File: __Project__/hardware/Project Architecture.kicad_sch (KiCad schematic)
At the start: 0 parts

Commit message: Different fixes and new footprints
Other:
- note added: "Page 7"
- note added: "Page 8"
- note removed: "Page 4"
- note removed: "Page 5"
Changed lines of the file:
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@@
 		)
 	)
-	(text "Page 5"
+	(text "Page 8"
 		(exclude_from_sim no)
 		(at 226.06 133.35 0)
@@
 			)
 			(justify right bottom)
-			(href "#5")
+			(href "#8")
 		)
 	)
-	(text "Page 4"
+	(text "Page 7"
 		(exclude_from_sim no)
 		(at 226.06 95.25 0)
@@
 			)
 			(justify right bottom)
-			(href "#4")
+			(href "#7")
 		)
 	)

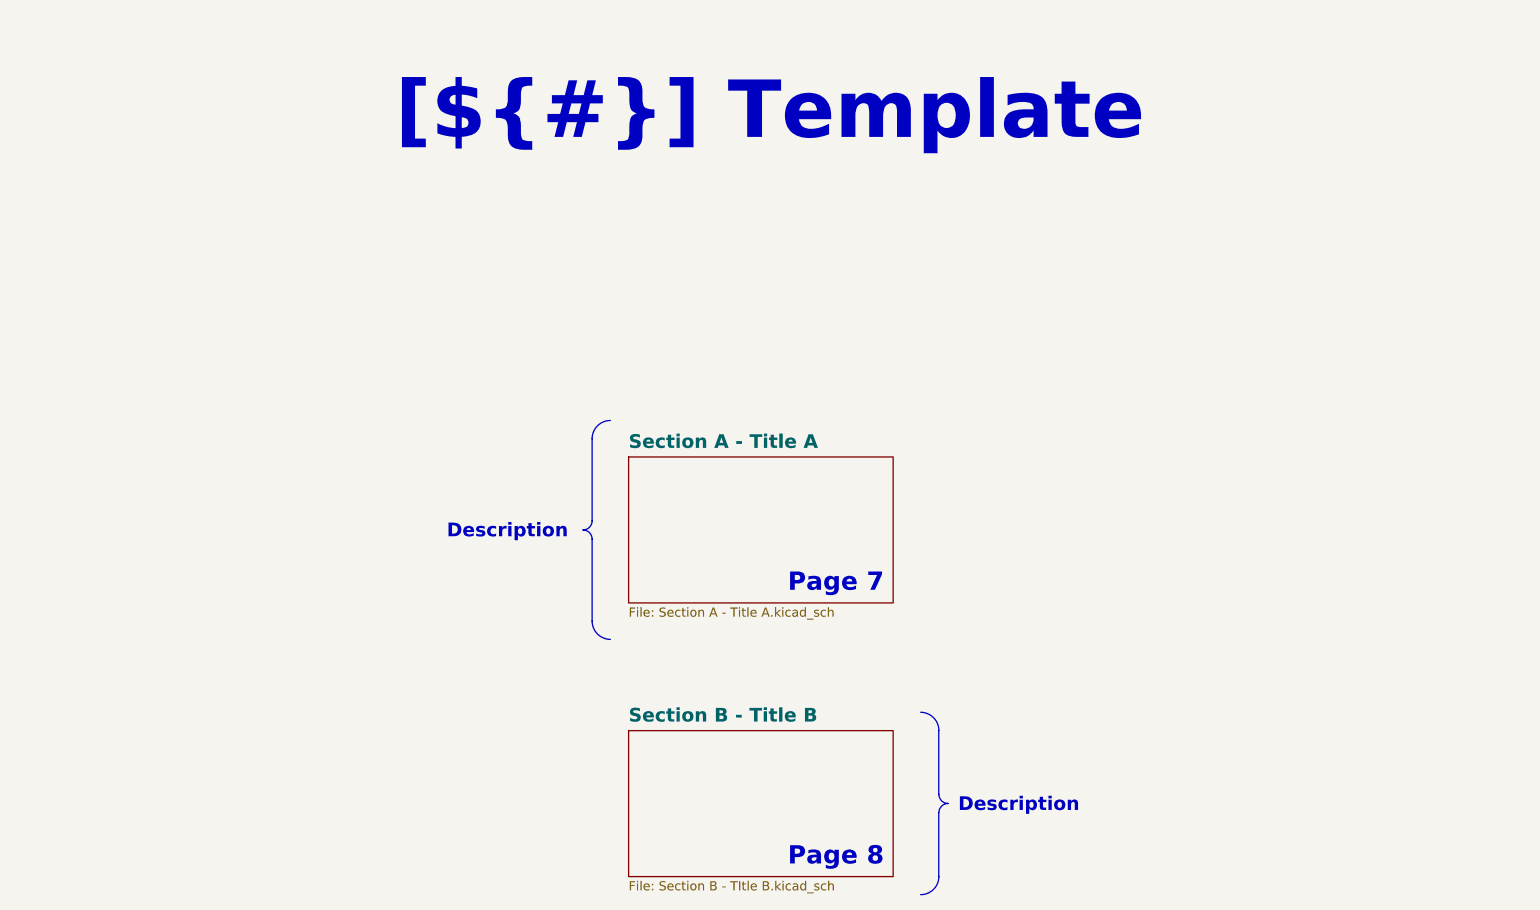
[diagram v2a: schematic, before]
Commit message: Fix JST footprints
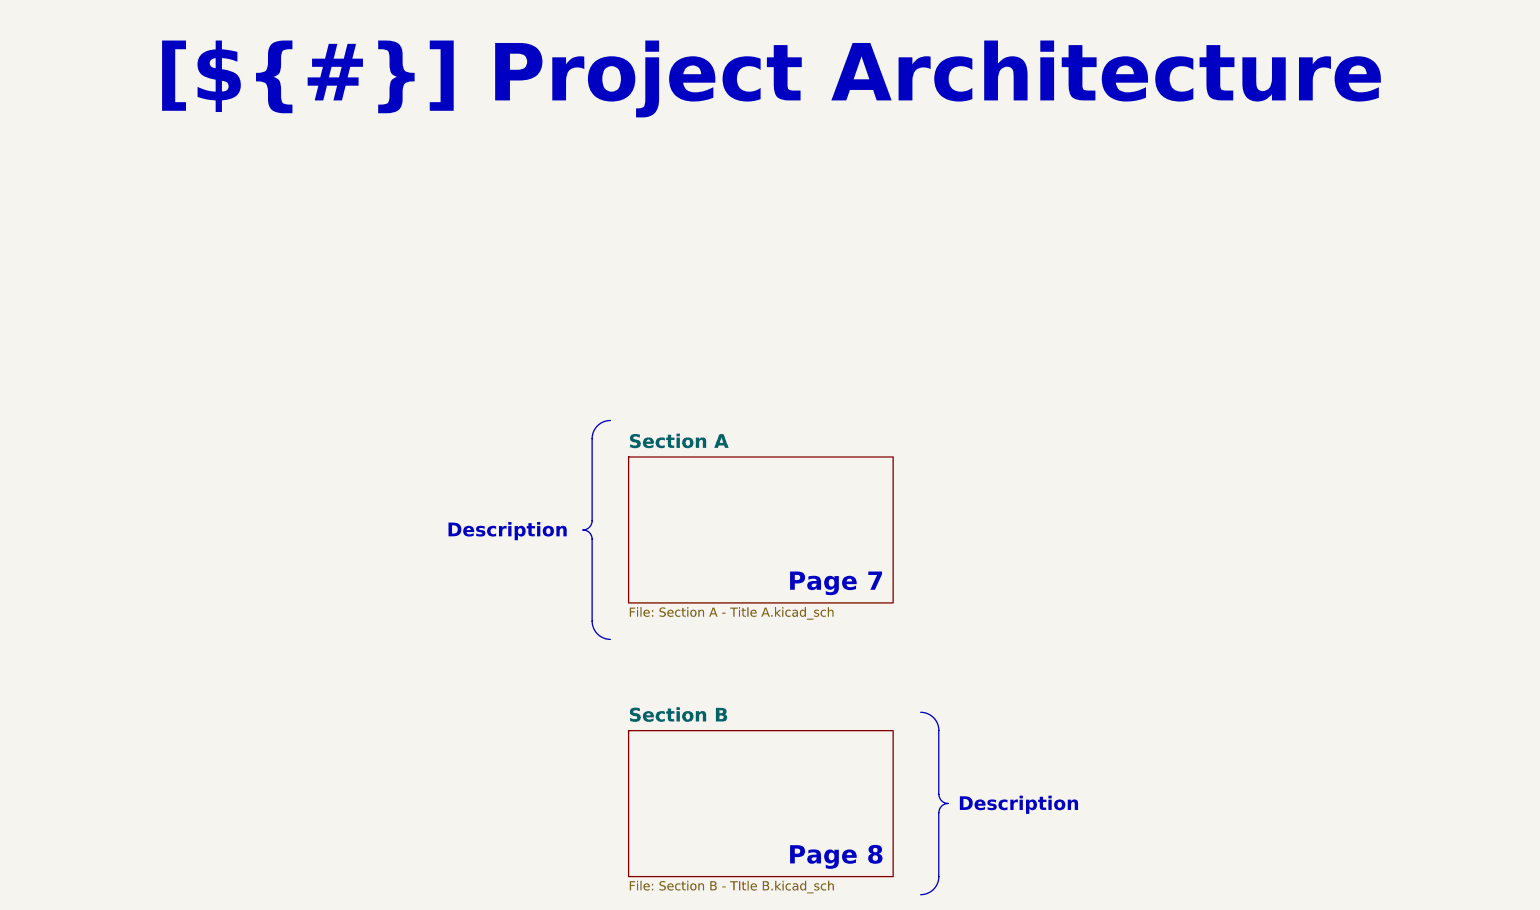
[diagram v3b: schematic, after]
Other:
- sheet Section A - Title A renamed Section A
- sheet Section B - Title B renamed Section B
- title: Template -> Project Architecture
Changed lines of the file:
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@@
 	(paper "A3")
 	(title_block
-		(title "Template")
+		(title "Project Architecture")
 		(date "2025-06-05")
 		(rev "${REVISION}")
@@
 		)
 	)
+	(text_box "[${#}] ${TITLE}"
+		(exclude_from_sim no)
+		(at 12.7 12.7 0)
+		(size 394.97 20.32)
+		(margins 5.9999 5.9999 5.9999 5.9999)
+		(stroke
+			(width -0.0001)
+			(type default)
+		)
+		(fill
+			(type none)
+		)
+		(effects
+			(font
+				(face "Times New Roman")
+				(size 8 8)
+				(thickness 1.2)
+				(bold yes)
+				(color 162 22 34 1)
+			)
+		)
+	)
 	(text_box "Description"
 		(exclude_from_sim no)
@@
 			)
 			(justify left top)
-		)
-	)
-	(text_box "[${#}] ${TITLE}"
-		(exclude_from_sim no)
-		(at 144.78 21.59 0)
-		(size 130.81 12.7)
-		(margins 5.9999 5.9999 5.9999 5.9999)
-		(stroke
-			(width -0.0001)
-			(type default)
-		)
-		(fill
-			(type none)
-		)
-		(effects
-			(font
-				(face "Times New Roman")
-				(size 8 8)
-				(thickness 1.2)
-				(bold yes)
-				(color 162 22 34 1)
-			)
 		)
 	)
@@
 			(color 255 200 0 0.5020)
 		)
-		(property "Sheetname" "Section B - Title B"
+		(property "Sheetname" "Section B"
 			(at 190.5 113.2709 0)
 			(effects
@@
 			(color 128 255 128 0.5000)
 		)
-		(property "Sheetname" "Section A - Title A"
+		(property "Sheetname" "Section A"
 			(at 190.5 75.1709 0)
 			(effects
